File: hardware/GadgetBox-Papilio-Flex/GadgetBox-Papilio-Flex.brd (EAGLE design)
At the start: 93.5 x 53.5 mm, 53 parts, among them SW1 SPST_TACT-KMR2, U1 MCP73831T-2ACI/OT, U5 LTC3419EMS, U7 FLASH-SPI-25XXSMD1, U8 6SLX9TQG144

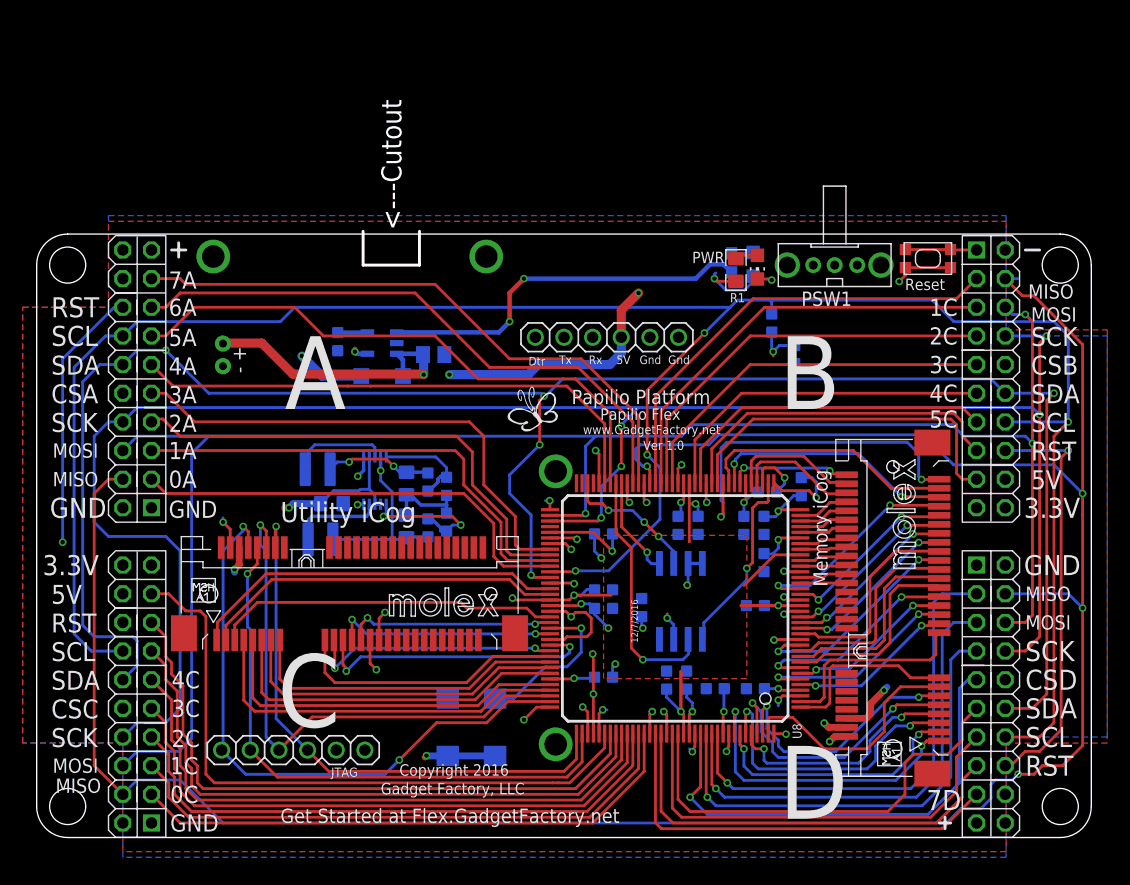
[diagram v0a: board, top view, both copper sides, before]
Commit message: Updated numbering scheme
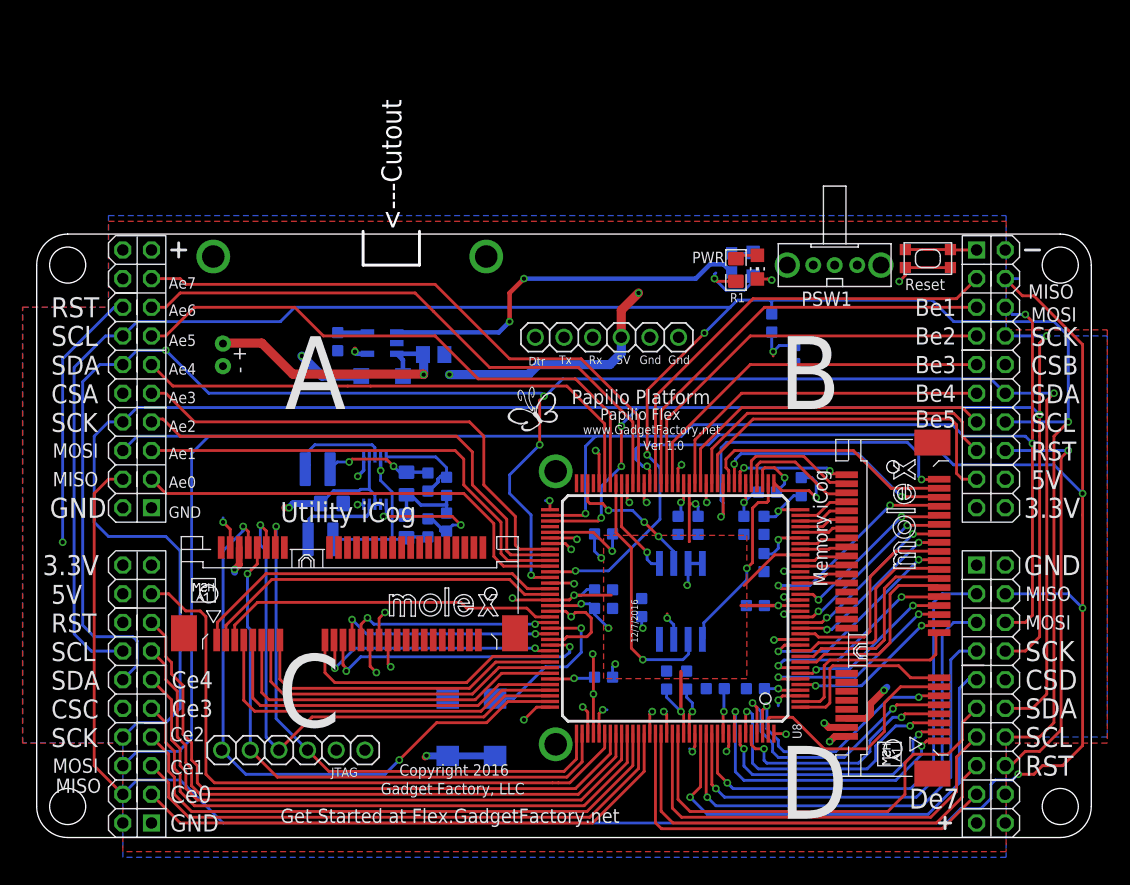
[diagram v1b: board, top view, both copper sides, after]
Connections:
- removed net N$18: ICU.31
- net SPI-CSC: now also ICU.31
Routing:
- net SPI-CSC: track 44.3 -> 70.1 mm, vias 1 -> 2
- net RX: track 59.0 -> 59.8 mm
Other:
- board text added: "Ae0"
- board text added: "Ae1"
- board text added: "Ae2"
- board text added: "Ae3"
- board text added: "Ae4"
- board text added: "Ae5"
- board text added: "Ae6"
- board text added: "Ae7"
- board text added: "Be1"
- board text added: "Be2"
- board text added: "Be3"
- board text added: "Be4"
- board text added: "Be5"
- board text added: "Ce0"
- board text added: "Ce1"
- board text added: "Ce2"
- board text added: "Ce3"
- board text added: "Ce4"
- board text added: "De7"
- board text removed: "0A"
- board text removed: "0C"
- board text removed: "1A"
- board text removed: "1C"
- board text removed: "2A"
- board text removed: "2C"
- board text removed: "3A"
- board text removed: "3C"
- board text removed: "4A"
- board text removed: "4C"
- board text removed: "5A"
- board text removed: "5C"
- board text removed: "6A"
- board text removed: "7A"
- board text removed: "7D"
